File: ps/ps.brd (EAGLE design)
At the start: 99.1 x 54.6 mm, 70 parts, among them IC1 LM675, Q1 NPN-D, Q2 NPN-D, U2 LM317, U3 TLC555CD, U4 LM317, U5 LM317

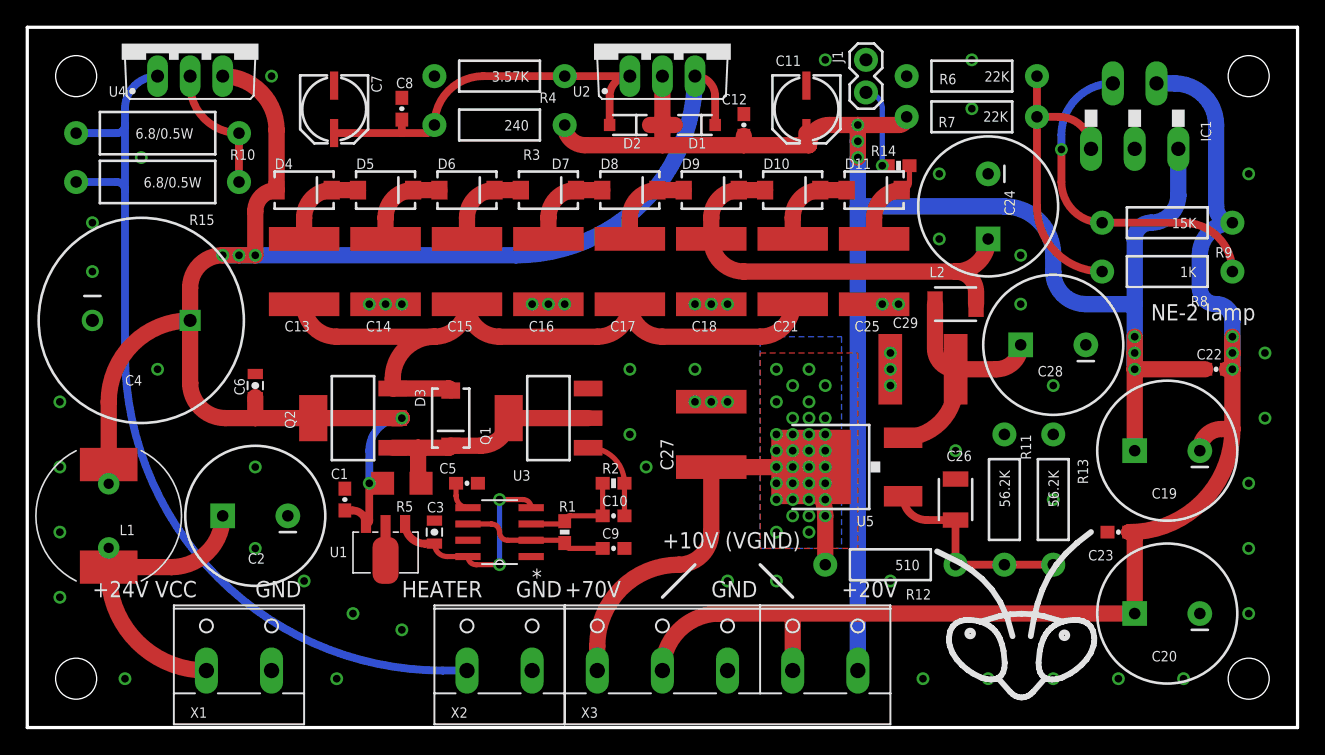
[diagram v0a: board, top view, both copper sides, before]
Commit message: PS rerouted
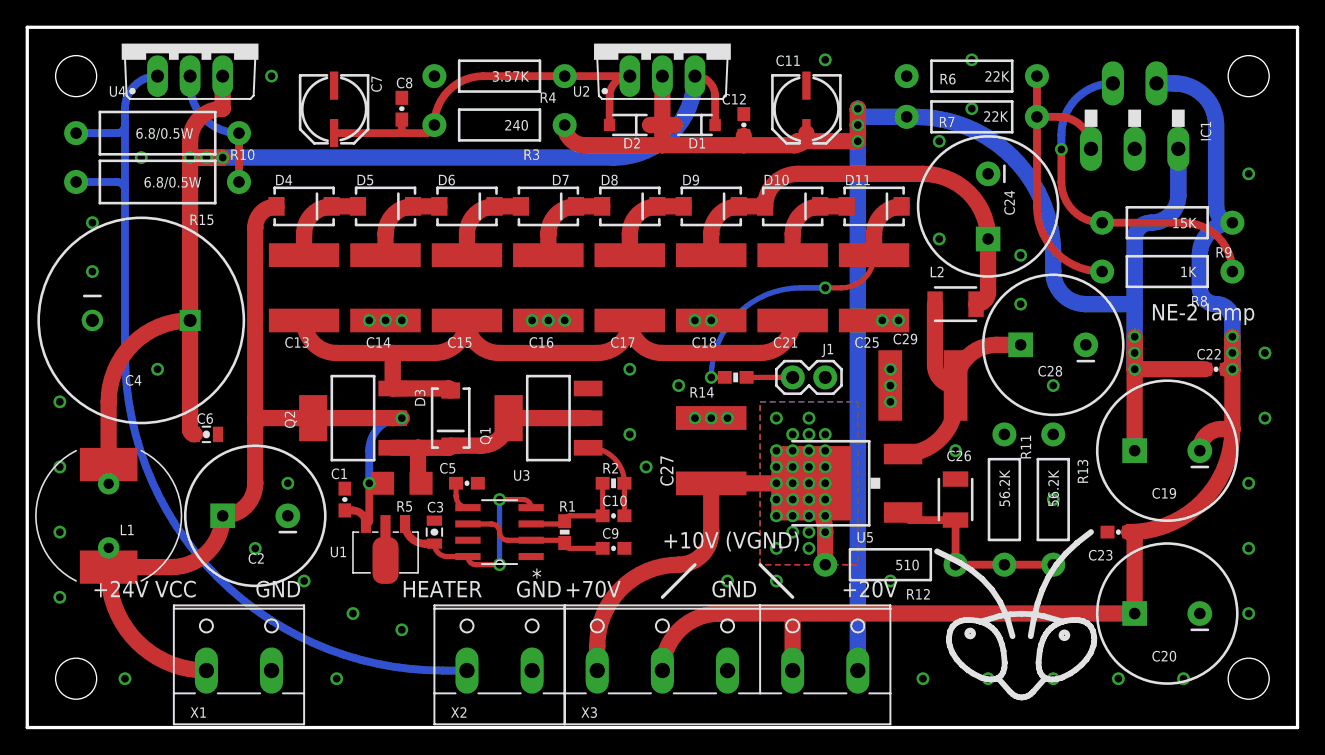
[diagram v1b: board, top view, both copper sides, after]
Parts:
- moved J1 25.0 mm to (62.2, 27.3), turned to 180 degrees
- moved R14 20.8 mm to (55.2, 27.3), turned to 180 degrees
- moved C6 5.39 mm to (14.0, 22.9), turned to 0 degrees
- moved C13 1.27 mm to (21.6, 34.3)
- moved C14 1.27 mm to (27.9, 34.3)
- moved C15 1.27 mm to (34.3, 34.3)
- moved C16 1.27 mm to (40.6, 34.3)
- moved C17 1.27 mm to (47.0, 34.3)
- moved C18 1.27 mm to (53.3, 34.3)
- moved C21 1.27 mm to (59.7, 34.3)
- moved C25 1.27 mm to (66.0, 34.3)
- moved C27 1.27 mm to (53.3, 21.6)
- moved C29 1.27 mm to (69.8, 26.7)
- moved U5 1.27 mm to (63.5, 19.1)
- moved D10 1.27 mm to (59.7, 40.6)
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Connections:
- net VCC: now also C1.1, D4.A, Q2.2, Q2.4, R5.2, U1.3
- net VINF: no longer C1.1, D4.A, Q2.2, Q2.4, R5.2, U1.3
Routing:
- net VCC: track 23.3 -> 73.3 mm, vias 0 -> 2
- net VINF: track 125.4 -> 93.5 mm, vias 5 -> 3
- net HV: track 6.85 -> 22.4 mm, vias 0 -> 2
- net N$5: track 6.66 -> 3.59 mm, vias 1 -> 0
- net PUMPIN: track 54.6 -> 52.0 mm
- net HT: track 33.8 -> 31.3 mm, vias 34 -> 30
- net N$7: track 18.6 -> 20.4 mm
- net N$15: track 33.6 -> 32.8 mm
- net N$18: track 16.0 -> 15.4 mm

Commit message: Separated grounds
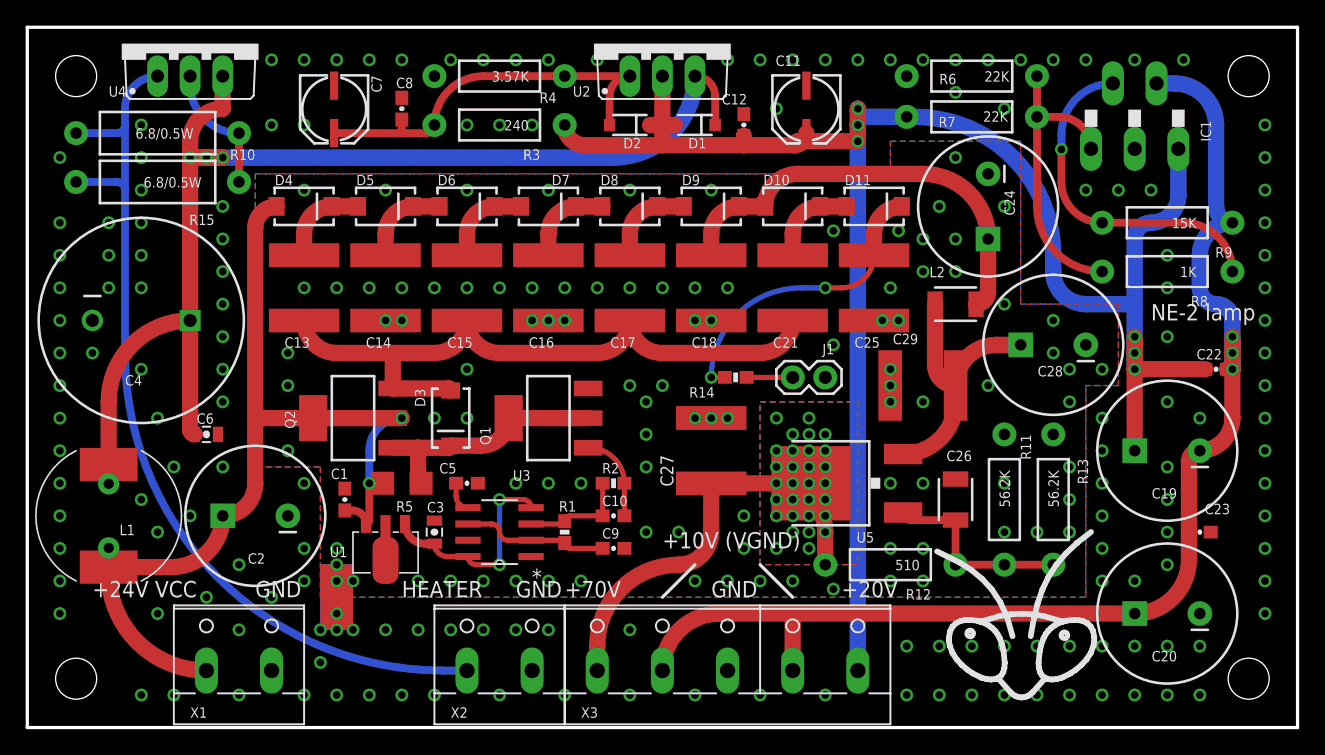
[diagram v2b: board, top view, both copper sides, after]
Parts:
- added GB1: COPPER-BRIDGE, my:COPPER-BRIDGE
- moved C23 6.35 mm to (91.4, 15.2), turned to 0 degrees
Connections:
- new net AGND: C11.-, C12.2, C2.-, C20.-, C23.2, C4.2, C6.2, C7.-, C8.2, GB1.P$2.1, GB1.P$2.2, IC1.3, R4.P$2, R7.P$2, X1.2, X2.2, X3.3
- net GND: now also GB1.P$1.1, GB1.P$1.2; no longer C11.-, C12.2, C2.-, C20.-, C23.2, C4.2, C6.2, C7.-, C8.2, IC1.3, R4.P$2, R7.P$2, U3.1, X1.2, X2.2, X3.3
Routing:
- net VGND: track 99.5 -> 96.0 mm
- added copper zone on layer 1, net AGND
- added copper zone on layer 16, net AGND

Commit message: More tweaks
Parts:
- J1: value (none) -> NE-2
- moved C22 4.02 mm to (88.9, 29.2)
- moved C23 1.27 mm to (92.7, 15.2)
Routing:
- net VREG: track 141.0 -> 119.4 mm, vias 6 -> 3
- net VGND: track 96.0 -> 100.6 mm, vias 3 -> 5
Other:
- board text removed: "NE-2 lamp"

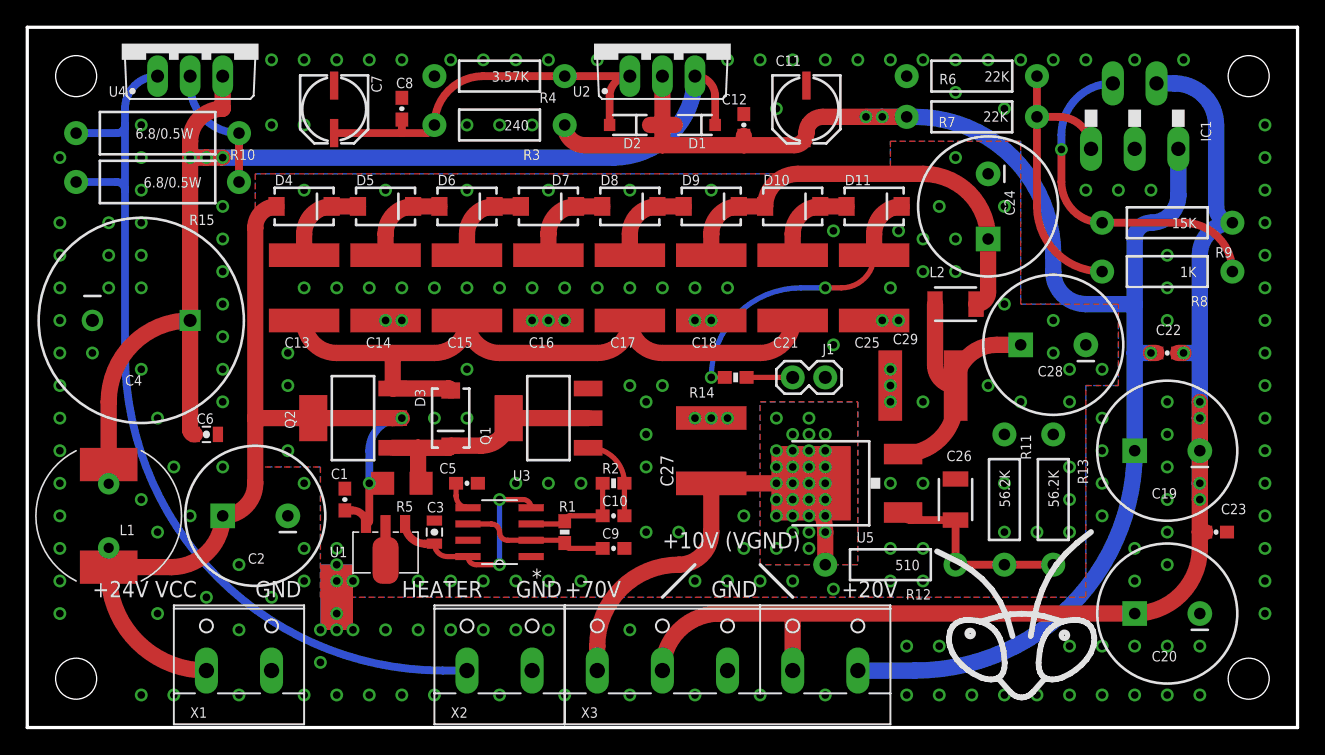
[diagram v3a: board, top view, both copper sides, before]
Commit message: LC damping resistors added to PS
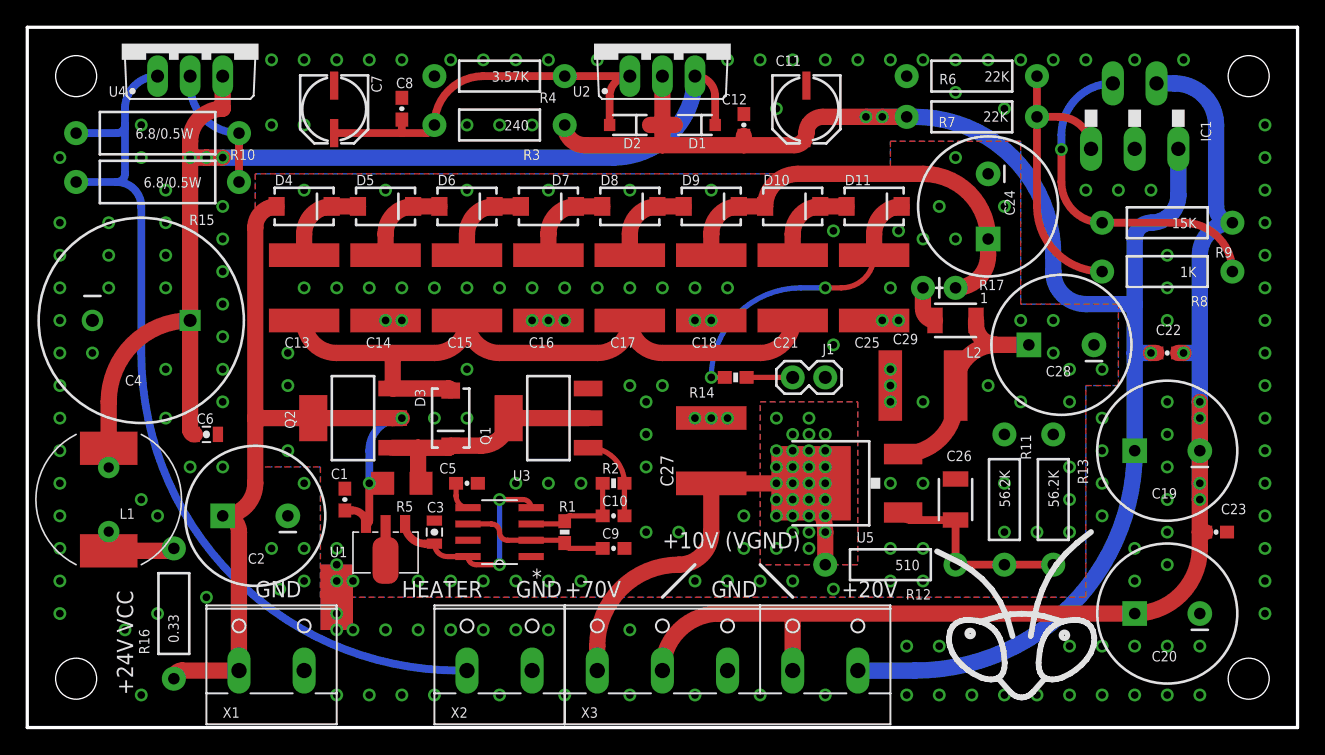
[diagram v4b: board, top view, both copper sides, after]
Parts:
- added R16: 0.33, SparkFun-Resistors:AXIAL-0.4
- added R17: 1, SparkFun-Resistors:AXIAL-0.1
- moved X1 2.54 mm to (19.1, 5.08)
- moved L2 1.27 mm to (72.4, 31.8), turned to 0 degrees
- moved L1 1.27 mm to (6.35, 17.8)
- moved C28 0.63 mm to (80.6, 29.8)
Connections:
- new net N$16: L2.1, R17.P$2
- new net N$9: L1.P$1, L1.P$1.1, R16.P$2
- net N$15: now also R17.P$1; no longer L2.1
- net VCC: now also R16.P$1; no longer L1.P$1, L1.P$1.1
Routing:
- net N$9: track 0.00 -> 6.66 mm
- net VCC: track 73.3 -> 68.0 mm
- net N$7: track 20.4 -> 16.6 mm
- net N$16: track 0.00 -> 2.93 mm
- net VINF: track 93.5 -> 92.2 mm
- net H+: track 67.7 -> 66.6 mm
- net N$15: track 32.8 -> 32.1 mm

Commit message: Unneeded caps removed
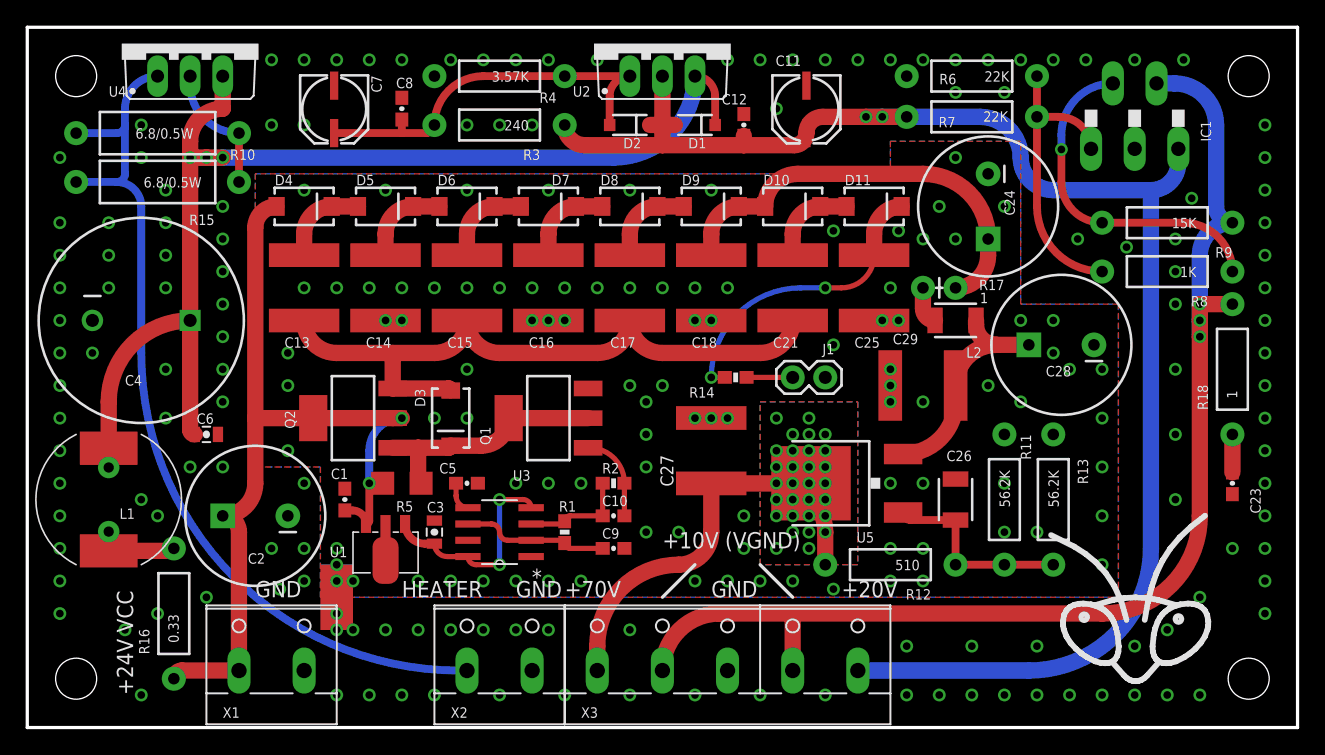
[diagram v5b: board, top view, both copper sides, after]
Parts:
- removed C19, C20: 470uF, SparkFun-Capacitors:CPOL-RADIAL-1000UF-25V
- removed C22: 0.1uF, SparkFun-Capacitors:0603-CAP
- added R18: 1, SparkFun-Resistors:AXIAL-0.4
- C23: value 0.1uF -> 0.22uF
- moved LOGO1 8.98 mm to (86.4, 10.2)
- moved C23 4.02 mm to (94.0, 19.1), turned to 270 degrees
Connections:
- new net N$17: C23.1, R18.P$1
- net AGND: no longer C20.-
- net VGND: now also R18.P$2; no longer C19.-, C20.+, C22.2, C23.1
- net VREG: no longer C19.+, C22.1
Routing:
- net VGND: track 100.6 -> 94.5 mm, vias 5 -> 3
- net N$17: track 0.00 -> 2.96 mm
- net VREG: track 119.4 -> 119.7 mm, vias 3 -> 2
